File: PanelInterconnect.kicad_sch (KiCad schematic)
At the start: 0 parts

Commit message: Starting layout
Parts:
- added J1: Conn_01x02, TerminalBlock:TerminalBlock_MaiXu_MX126-5.0-02P_1x02_P5.00mm, symbol Connector_Generic:Conn_01x02
- added J2: Conn_01x04, TerminalBlock:TerminalBlock_MaiXu_MX126-5.0-04P_1x04_P5.00mm, symbol Connector_Generic:Conn_01x04
- added SC1, SC10, SC11, SC12, SC2, SC3, SC4, SC5, SC6, SC7, SC8, SC9: Solar_Cell, _PanelInterconnct:maxeon_c60, symbol Device:Solar_Cell
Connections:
- new net: SC10.2 (-), SC11.1 (+)
- new net: SC11.2 (-), SC12.1 (+)
- new net: SC3.2 (-), SC4.1 (+)
- new net: SC4.2 (-), SC5.1 (+)
- new net: J1.1 (Pin_1), J2.1 (Pin_1)
- new net: J1.2 (Pin_2), J2.2 (Pin_2)
- new net: J2.3 (Pin_3), SC1.1 (+)
- new net: J2.4 (Pin_4), SC12.2 (-)
- new net: SC10.1 (+), SC9.2 (-)
- new net: SC6.2 (-), SC7.1 (+)
- new net: SC7.2 (-), SC8.1 (+)
- new net: SC1.2 (-), SC2.1 (+)
- new net: SC2.2 (-), SC3.1 (+)
- new net: SC5.2 (-), SC6.1 (+)
- new net: SC8.2 (-), SC9.1 (+)
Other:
- company: (none) -> Solar Plane
- title: (none) -> Solar Panel Interconnects

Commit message: Pushing
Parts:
- removed J1: Conn_01x02, TerminalBlock:TerminalBlock_MaiXu_MX126-5.0-02P_1x02_P5.00mm, symbol Connector_Generic:Conn_01x02
- removed J2: Conn_01x04, TerminalBlock:TerminalBlock_MaiXu_MX126-5.0-04P_1x04_P5.00mm, symbol Connector_Generic:Conn_01x04
- added J2: Conn_01x06, Connector_FFC-FPC:Jushuo_AFC07-S06FCA-00_1x6-1MP_P0.50_Horizontal, symbol Connector_Generic:Conn_01x06
- added J3: Conn_01x30, _PanelInterconnct:FPC_30x01, symbol Connector_Generic:Conn_01x30
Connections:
- net at SC1.1 (+): now also J2.4 (Pin_4), J2.5 (Pin_5), J2.6 (Pin_6), J3.15 (Pin_15), J3.16 (Pin_16), J3.17 (Pin_17), J3.18 (Pin_18), J3.19 (Pin_19), J3.20 (Pin_20), J3.21 (Pin_21), J3.22 (Pin_22), J3.23 (Pin_23), J3.24 (Pin_24), J3.25 (Pin_25), J3.26 (Pin_26), J3.27 (Pin_27)
- net at SC12.2 (-): now also J3.1 (Pin_1), J3.10 (Pin_10), J3.11 (Pin_11), J3.12 (Pin_12), J3.13 (Pin_13), J3.2 (Pin_2), J3.3 (Pin_3), J3.4 (Pin_4), J3.5 (Pin_5), J3.6 (Pin_6), J3.7 (Pin_7), J3.8 (Pin_8), J3.9 (Pin_9)
- new net: J2.1 (Pin_1), J2.2 (Pin_2), J2.3 (Pin_3), J3.29 (Pin_29), J3.30 (Pin_30)
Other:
- moved on the sheet: SC1, SC10, SC11, SC12, SC2, SC3, SC4, SC5, SC6, SC7, SC8, SC9

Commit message: Still working on it
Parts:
- removed J2: Conn_01x06, Connector_FFC-FPC:Jushuo_AFC07-S06FCA-00_1x6-1MP_P0.50_Horizontal, symbol Connector_Generic:Conn_01x06
- removed SC10, SC11, SC12, SC9: Solar_Cell, _PanelInterconnct:maxeon_c60, symbol Device:Solar_Cell
- added J1: Conn_01x10, _PanelInterconnct:kyocera_fpc_01x10, symbol Connector_Generic:Conn_01x10
- J3: footprint _PanelInterconnct:FPC_30x01 -> _PanelInterconnct:kyocera_fpc_01x30
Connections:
- net at J3.15 (Pin_15), J3.16 (Pin_16), J3.17 (Pin_17)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: now also J1.4 (Pin_4), J1.5 (Pin_5), J1.6 (Pin_6)
- net at J3.1 (Pin_1), J3.10 (Pin_10), J3.11 (Pin_11)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: now also SC8.2 (-)
- net at J3.29 (Pin_29), J3.30 (Pin_30): now also J1.1 (Pin_1), J1.2 (Pin_2), J1.3 (Pin_3)
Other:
- moved on the sheet: J3, SC1, SC2, SC3, SC4, SC5, SC6, SC7, SC8

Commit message: Working on it still
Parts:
- SC1, SC2, SC3, SC4, SC5, SC6, SC7, SC8: value Solar_Cell -> Maxeon C60
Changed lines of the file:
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@@
 			)
 		)
-		(property "Value" "Solar_Cell"
+		(property "Value" "Maxeon C60"
 			(at 122.301 76.2 90)
 			(effects
@@
 			)
 		)
-		(property "Value" "Solar_Cell"
+		(property "Value" "Maxeon C60"
 			(at 164.211 76.2 90)
 			(effects
@@
 			)
 		)
-		(property "Value" "Solar_Cell"
+		(property "Value" "Maxeon C60"
 			(at 80.391 76.2 90)
 			(effects
@@
 			)
 		)
-		(property "Value" "Solar_Cell"
+		(property "Value" "Maxeon C60"
 			(at 94.361 76.2 90)
 			(effects
@@
 			)
 		)
-		(property "Value" "Solar_Cell"
+		(property "Value" "Maxeon C60"
 			(at 150.241 76.2 90)
 			(effects
@@
 			)
 		)
-		(property "Value" "Solar_Cell"
+		(property "Value" "Maxeon C60"
 			(at 136.271 76.2 90)
 			(effects
@@
 			)
 		)
-		(property "Value" "Solar_Cell"
+		(property "Value" "Maxeon C60"
 			(at 108.331 76.2 90)
 			(effects
@@
 			)
 		)
-		(property "Value" "Solar_Cell"
+		(property "Value" "Maxeon C60"
 			(at 178.181 76.2 90)
 			(effects

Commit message: Cleaning up layout
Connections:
- net at SC4.1 (+): now also SC5.2 (-); no longer SC3.2 (-)
- net at SC4.2 (-): now also SC3.1 (+); no longer SC5.1 (+)
- net at SC7.1 (+): now also SC8.2 (-); no longer SC6.2 (-)
- net at SC7.2 (-): now also SC6.1 (+); no longer SC8.1 (+)
- net at J1.5 (Pin_5), J1.6 (Pin_6), J3.15 (Pin_15)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: now also J1.10 (Pin_10), J1.7 (Pin_7), J1.8 (Pin_8), J1.9 (Pin_9), SC1.2 (-); no longer J1.4 (Pin_4), SC1.1 (+)
- net at SC2.1 (+): now also SC3.2 (-); no longer SC1.2 (-)
- net at SC2.2 (-): now also SC1.1 (+); no longer SC3.1 (+)
- net at J3.1 (Pin_1), J3.10 (Pin_10), J3.11 (Pin_11)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: now also SC8.1 (+); no longer SC8.2 (-)
- new net: SC5.1 (+), SC6.2 (-)
- no-connect marks 0 -> 1
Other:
- moved on the sheet: SC1, SC2, SC3, SC4, SC5, SC6, SC7, SC8

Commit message: Finishing up backup interconnects
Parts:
- removed J3: Conn_01x30, _PanelInterconnct:kyocera_fpc_01x30, symbol Connector_Generic:Conn_01x30
- removed SC3, SC4, SC5, SC6, SC7, SC8: Maxeon C60, _PanelInterconnct:maxeon_c60, symbol Device:Solar_Cell
- J1: footprint _PanelInterconnct:kyocera_fpc_01x10 -> _PanelInterconnects:tb4_10p
- SC1, SC2: footprint _PanelInterconnct:maxeon_c60 -> _PanelInterconnects:maxeon_c60
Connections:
- net at SC1.1 (+): now also J1.1 (Pin_1), J1.2 (Pin_2), J1.3 (Pin_3), J1.4 (Pin_4), J1.5 (Pin_5); no longer SC2.2 (-)
- net at J1.10 (Pin_10), J1.6 (Pin_6), J1.7 (Pin_7)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: now also SC2.1 (+); no longer J1.5 (Pin_5), SC1.2 (-)
- new net: SC1.2 (-), SC2.2 (-)
- no-connect marks 1 -> 0
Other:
- moved on the sheet: SC1

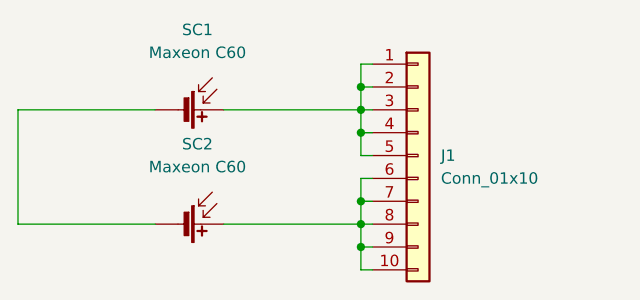
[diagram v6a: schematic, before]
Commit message: updated panel interconnect
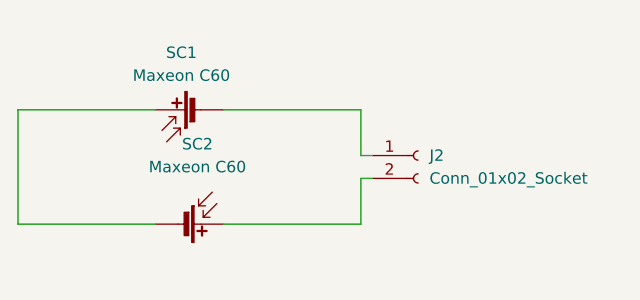
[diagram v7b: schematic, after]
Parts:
- removed J1: Conn_01x10, _PanelInterconnects:tb4_10p, symbol Connector_Generic:Conn_01x10
- added J2: Conn_01x02_Socket, Connector_AMASS:AMASS_XT30U-F_1x02_P5.0mm_Vertical, symbol Connector:Conn_01x02_Socket
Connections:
- net at SC1.1 (+): now also SC2.2 (-)
- net at SC2.1 (+): now also J2.2 (Pin_2)
- net at SC1.2 (-): now also J2.1 (Pin_1); no longer SC2.2 (-)
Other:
- moved on the sheet: SC1
